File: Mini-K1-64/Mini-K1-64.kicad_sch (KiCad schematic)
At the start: 3 parts

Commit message: Format PCB
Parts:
- renumbered H2 to H1, H1 to H2
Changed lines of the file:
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@@
 		(on_board yes)
 		(dnp no)
-		(property "Reference" "H2"
+		(property "Reference" "H1"
 			(at 58.42 120.142 0)
 			(effects
@@
 			(project "Mini-K1-64"
 				(path "/1a7e0d91-a6c0-4b42-a7c6-42574ab26c7c"
-					(reference "H2")
+					(reference "H1")
 					(unit 1)
 				)
@@
 		(on_board yes)
 		(dnp no)
-		(property "Reference" "H1"
+		(property "Reference" "H2"
 			(at 58.42 127.762 0)
 			(effects
@@
 			(project "Mini-K1-64"
 				(path "/1a7e0d91-a6c0-4b42-a7c6-42574ab26c7c"
-					(reference "H1")
-					(unit 1)
-				)
+					(reference "H2")
+					(unit 1)
+				)

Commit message: Add Symbol
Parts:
- added LOGO1: ~, WTMEC:WTLogo, symbol MCU_NXP_S32K1:WTLogo
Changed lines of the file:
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@@
+	)
+	(symbol
+		(lib_id "MCU_NXP_S32K1:WTLogo")
+		(at 58.42 144.78 0)
+		(unit 1)
+		(exclude_from_sim no)
+		(in_bom yes)
+		(on_board yes)
+		(dnp no)
+		(fields_autoplaced yes)
+		(property "Reference" "LOGO1"
+			(at 60.706 139.954 0)
+			(effects
+				(font
+					(size 1.27 1.27)
+				)
+				(hide yes)
+			)
+		)
+		(property "Value" "~"
+			(at 58.42 144.78 0)
+			(effects
+				(font
+					(size 1.27 1.27)
+				)
+				(hide yes)
+			)
+		)
+		(property "Footprint" "WTMEC:WTLogo"
+			(at 65.278 146.304 0)
+			(effects
+				(font
+					(size 1.27 1.27)
+				)
+				(hide yes)
+			)
+		)
+		(property "Datasheet" ""
+			(at 58.42 144.78 0)
+			(effects
+				(font
+					(size 1.27 1.27)
+				)
+				(hide yes)
+			)
+		)
+		(property "Description" ""
+			(at 58.42 144.78 0)
+			(effects
+				(font
+					(size 1.27 1.27)
+				)
+				(hide yes)
+			)
+		)
+		(instances
+			(project "Mini-K1-64"
+				(path "/1a7e0d91-a6c0-4b42-a7c6-42574ab26c7c"
+					(reference "LOGO1")
+					(unit 1)
+				)
+			)
+		)
 	)
 	(symbol

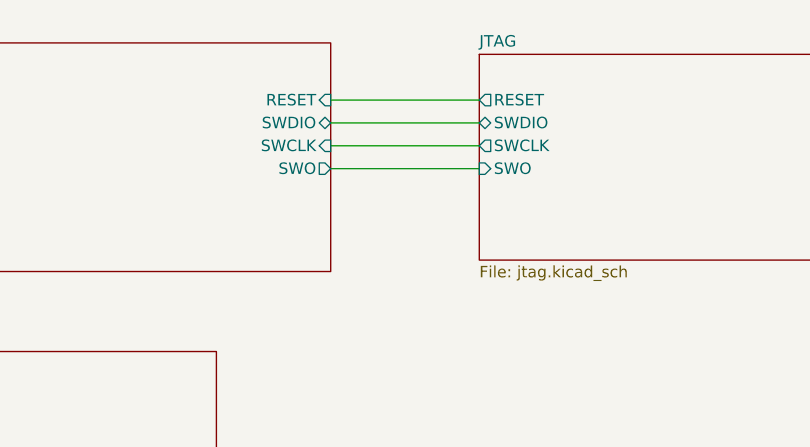
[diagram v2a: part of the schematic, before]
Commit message: Update Debug Connector
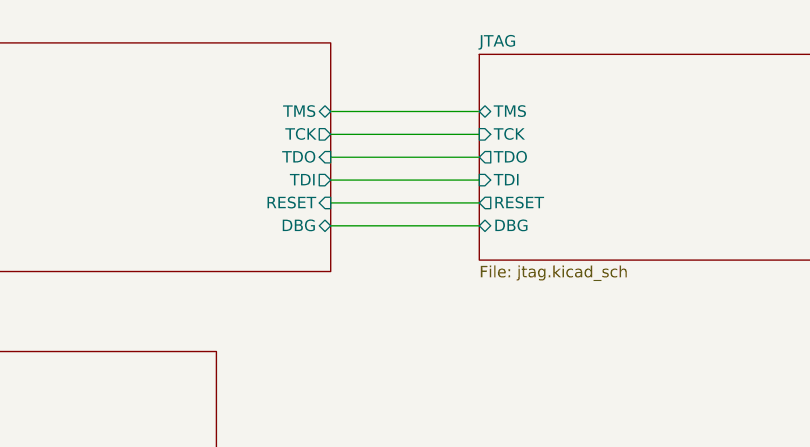
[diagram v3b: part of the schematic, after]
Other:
- sheet JTAG ports: added DBG, TCK, TDI, TDO, TMS; removed SWCLK, SWDIO, SWO
- sheet MCU ports: added DBG, TCK, TDI, TDO, TMS; removed SWCLK, SWDIO, SWO
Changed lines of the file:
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@@
-	(wire
-		(pts
-			(xy 184.15 76.2) (xy 200.66 76.2)
-		)
-		(stroke
-			(width 0)
-			(type default)
-		)
-	)
-	(wire
-		(pts
-			(xy 184.15 81.28) (xy 200.66 81.28)
-		)
-		(stroke
-			(width 0)
-			(type default)
-		)
-	)
 	(wire
 		(pts
@@
 	(wire
 		(pts
+			(xy 184.15 80.01) (xy 200.66 80.01)
+		)
+		(stroke
+			(width 0)
+			(type default)
+		)
+	)
+	(wire
+		(pts
 			(xy 67.31 132.08) (xy 67.31 129.54)
 		)
@@
 	(wire
 		(pts
-			(xy 184.15 78.74) (xy 200.66 78.74)
+			(xy 184.15 74.93) (xy 200.66 74.93)
+		)
+		(stroke
+			(width 0)
+			(type default)
+		)
+	)
+	(wire
+		(pts
+			(xy 184.15 82.55) (xy 200.66 82.55)
+		)
+		(stroke
+			(width 0)
+			(type default)
+		)
+	)
+	(wire
+		(pts
+			(xy 184.15 85.09) (xy 200.66 85.09)
+		)
+		(stroke
+			(width 0)
+			(type default)
+		)
+	)
+	(wire
+		(pts
+			(xy 184.15 77.47) (xy 200.66 77.47)
 		)
 		(stroke
@@
 	(wire
 		(pts
-			(xy 184.15 73.66) (xy 200.66 73.66)
+			(xy 184.15 87.63) (xy 200.66 87.63)
 		)
 		(stroke
@@
 		)
 		(pin "RESET" input
-			(at 184.15 73.66 0)
+			(at 184.15 85.09 0)
 			(effects
 				(font
@@
 			)
 		)
-		(pin "SWCLK" input
-			(at 184.15 78.74 0)
+		(pin "TMS" bidirectional
+			(at 184.15 74.93 0)
 			(effects
 				(font
@@
 			)
 		)
-		(pin "SWDIO" bidirectional
-			(at 184.15 76.2 0)
+		(pin "TDO" input
+			(at 184.15 80.01 0)
 			(effects
 				(font
@@
 			)
 		)
-		(pin "SWO" output
-			(at 184.15 81.28 0)
+		(pin "DBG" bidirectional
+			(at 184.15 87.63 0)
+			(effects
+				(font
+					(size 1.27 1.27)
+				)
+				(justify right)
+			)
+		)
+		(pin "TCK" output
+			(at 184.15 77.47 0)
+			(effects
+				(font
+					(size 1.27 1.27)
+				)
+				(justify right)
+			)
+		)
+		(pin "TDI" output
+			(at 184.15 82.55 0)
 			(effects
 				(font
@@
 			)
 		)
-		(pin "SWDIO" bidirectional
-			(at 200.66 76.2 180)
+		(pin "TMS" bidirectional
+			(at 200.66 74.93 180)
 			(effects
 				(font
@@
 		)
 		(pin "RESET" output
-			(at 200.66 73.66 180)
+			(at 200.66 85.09 180)
 			(effects
 				(font
@@
 			)
 		)
-		(pin "SWCLK" output
-			(at 200.66 78.74 180)
+		(pin "DBG" bidirectional
+			(at 200.66 87.63 180)
 			(effects
 				(font
@@
 			)
 		)
-		(pin "SWO" input
-			(at 200.66 81.28 180)
-			(effects
-				(font
+		(pin "TCK" input
+			(at 200.66 77.47 180)
+			(effects
+				(font
+					(size 1.27 1.27)
+				)
+				(justify left)
+			)
+		)
+		(pin "TDO" output
+			(at 200.66 80.01 180)
+			(effects
+				(font
+					(size 1.27 1.27)
+				)
+				(justify left)
+			)
+		)
+		(pin "TDI" input
+			(at 200.66 82.55 180)
+			(effects
+				(font
